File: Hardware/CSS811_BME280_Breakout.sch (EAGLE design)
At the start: 24 parts, among them J1 JST, J2 CCS811 Options, J3 JST, J4 PTH, U2 CCS811

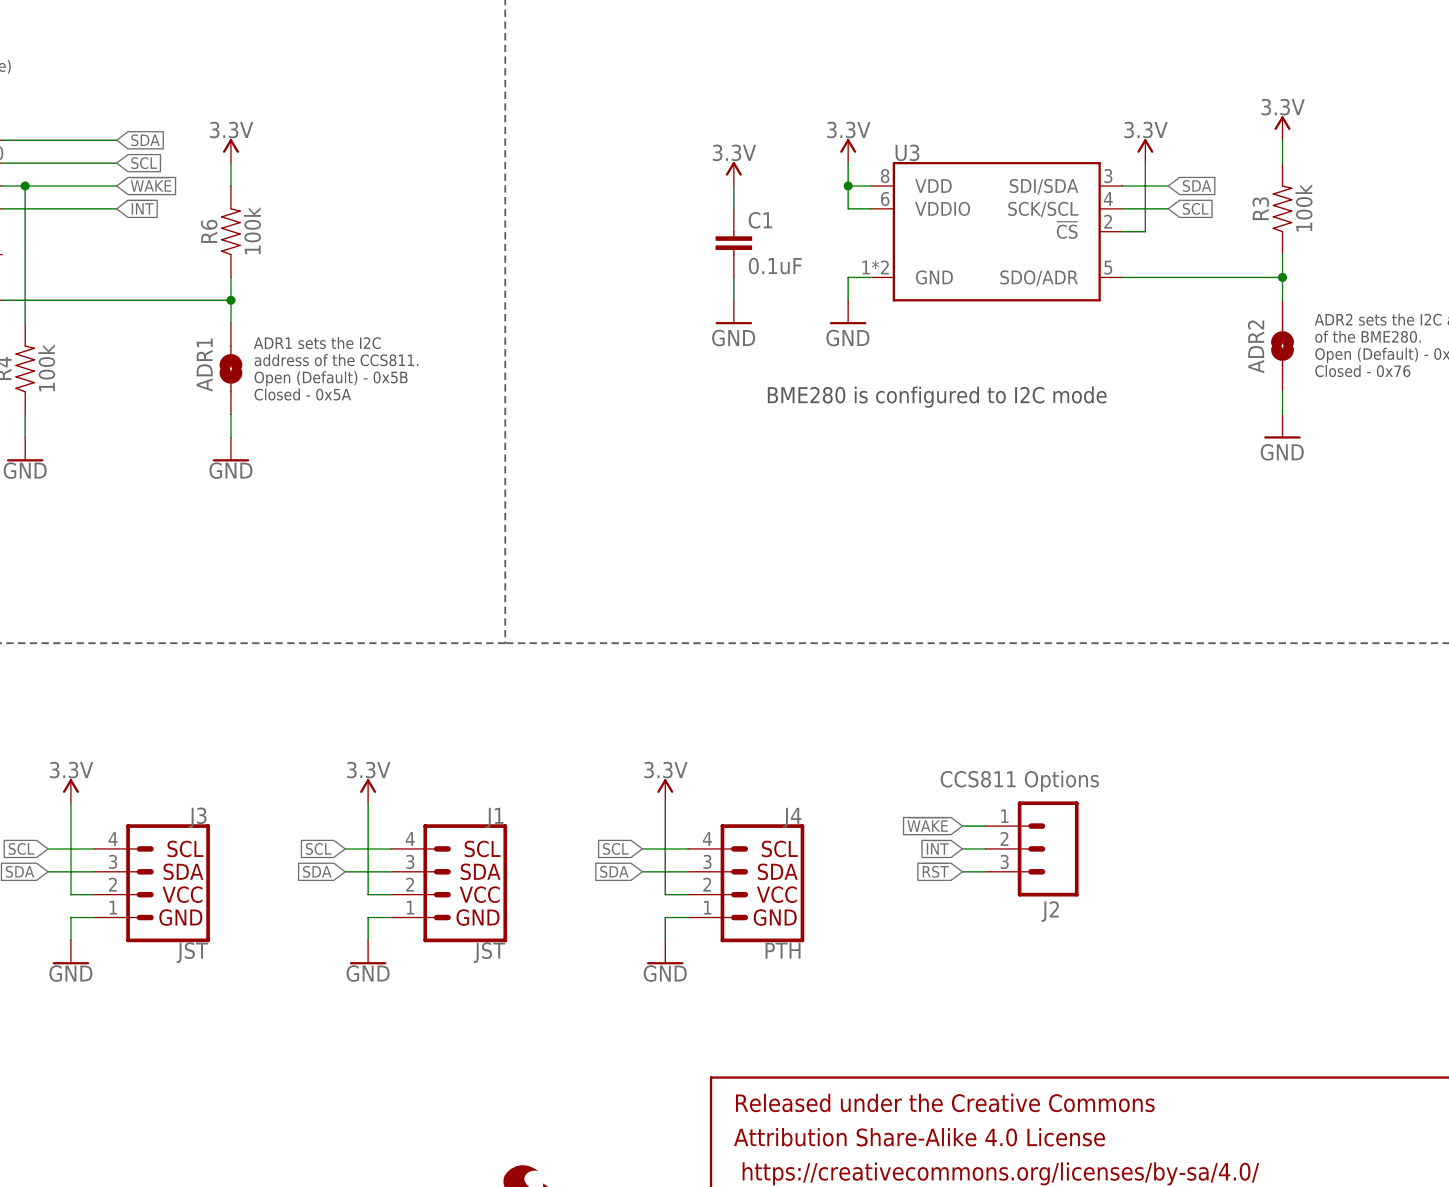
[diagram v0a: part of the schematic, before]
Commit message: Updated parts to fit with SFE library
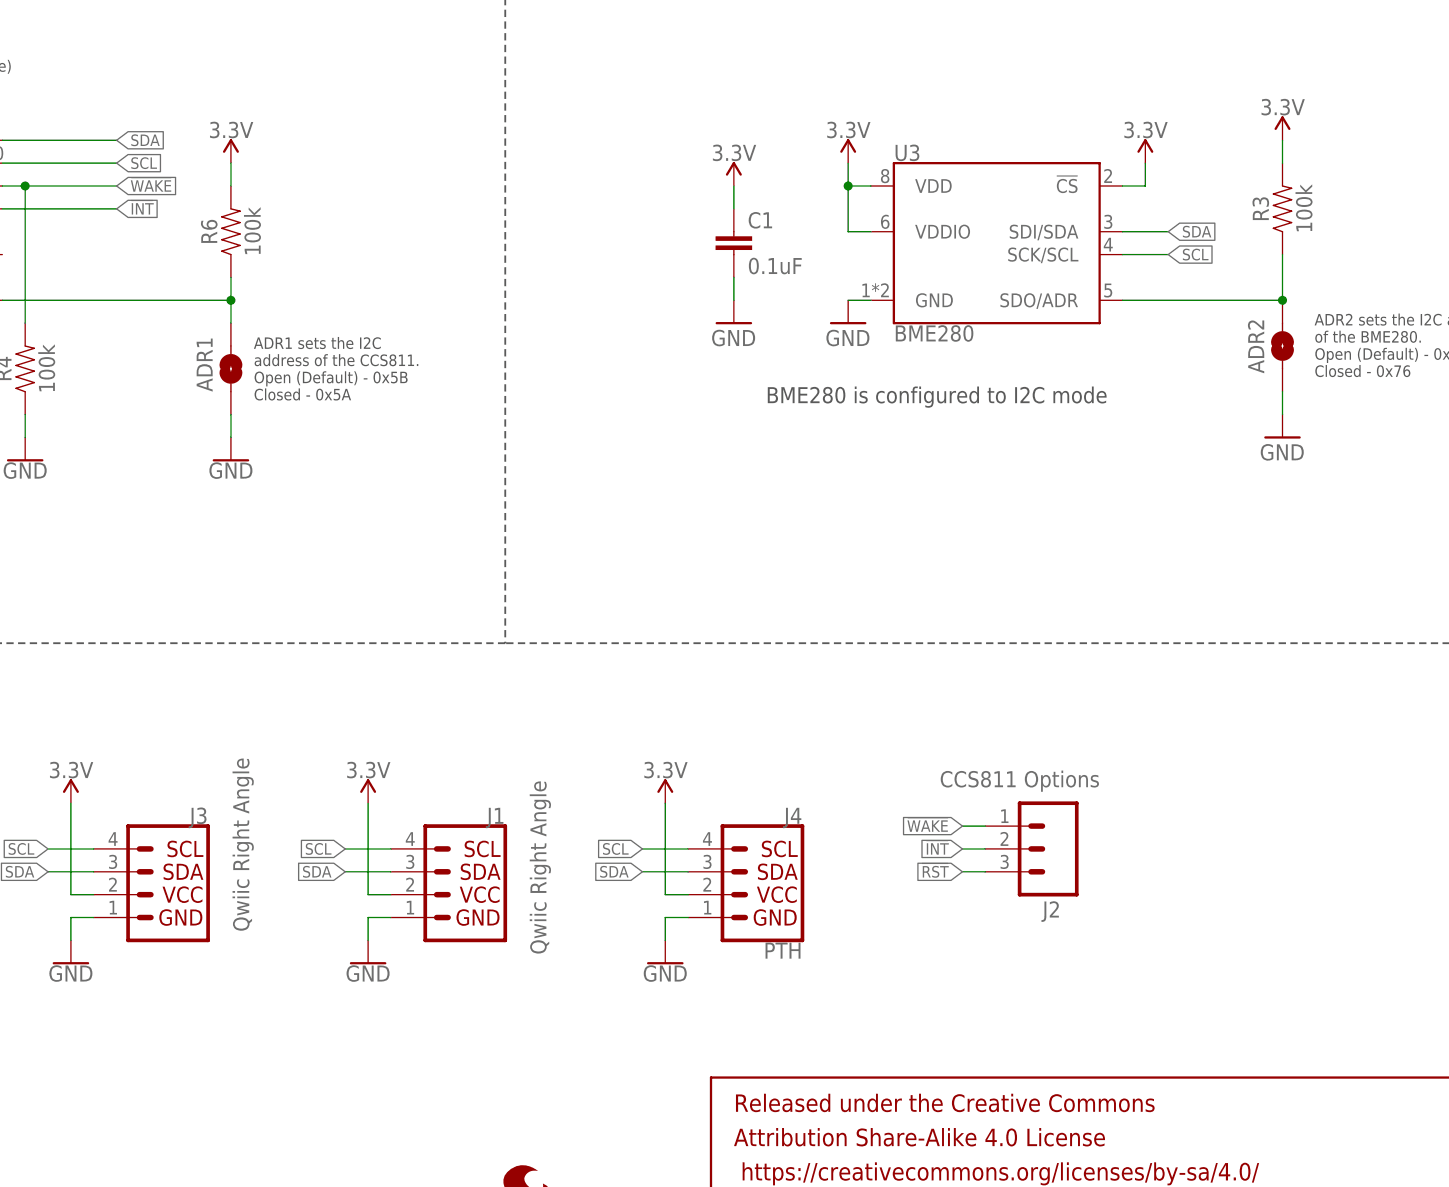
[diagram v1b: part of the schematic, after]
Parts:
- J1, J3: value JST -> Qwiic Right Angle; device SparkX:I2C_STANDARDJS-1MM -> SparkFun-Connectors:I2C_STANDARDQWIIC
- U2: device SparkX:CCS811PRODUCTION -> SparkFun-Sensors:CCS811PRODUCTION
- U3: value (none) -> BME280; device SparkX:BME280 -> SparkFun-Sensors:BME280
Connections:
- net 3.3V: now also J1.2, J3.2; no longer J1.VCC, J3.VCC
- net GND: now also J1.1, J3.1; no longer J1.GND, J3.GND
- net SCL: now also J1.4, J3.4; no longer J1.SCL, J3.SCL
- net SDA: now also J1.3, J3.3; no longer J1.SDA, J3.SDA
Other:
- moved on the sheet: U3
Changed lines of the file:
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@@
 <layer number="230" name="230bmp" color="7" fill="1" visible="yes" active="yes"/>
 <layer number="231" name="231bmp" color="7" fill="1" visible="yes" active="yes"/>
+<layer number="232" name="Eagle3D_PG2" color="7" fill="1" visible="yes" active="yes"/>
+<layer number="233" name="Eagle3D_PG3" color="7" fill="1" visible="yes" active="yes"/>
 <layer number="248" name="Housing" color="7" fill="1" visible="yes" active="yes"/>
 <layer number="249" name="Edge" color="7" fill="1" visible="yes" active="yes"/>
@@
 <part name="R2" library="SparkFun-Resistors" deviceset="4.7KOHM" device="-0603-1/10W-1%" value="4.7k"/>
 <part name="J2" library="SparkFun-Connectors" deviceset="CONN_03" device="1X03_NO_SILK" value="CCS811 Options"/>
-<part name="U2" library="SparkX" deviceset="CCS811" device="PRODUCTION" value="CCS811"/>
+<part name="U2" library="SparkFun-Sensors" deviceset="CCS811" device="PRODUCTION" value="CCS811"/>
 <part name="GND2" library="SparkFun-Aesthetics" deviceset="GND" device=""/>
 <part name="GND7" library="SparkFun-Aesthetics" deviceset="GND" device=""/>
@@
 <part name="SUPPLY12" library="SparkFun-PowerSymbols" deviceset="3.3V" device=""/>
 <part name="SUPPLY14" library="SparkFun-PowerSymbols" deviceset="3.3V" device=""/>
-<part name="U3" library="SparkX" deviceset="BME280" device=""/>
-<part name="J3" library="SparkX" deviceset="I2C_STANDARD" device="JS-1MM" value="JST"/>
+<part name="U3" library="SparkFun-Sensors" deviceset="BME280" device="" value="BME280"/>
+<part name="J3" library="SparkFun-Connectors" deviceset="I2C_STANDARD" device="QWIIC" value="Qwiic Right Angle"/>
 <part name="GND4" library="SparkFun-PowerSymbols" deviceset="GND" device=""/>
 <part name="SUPPLY1" library="SparkFun-PowerSymbols" deviceset="3.3V" device=""/>
@@
 <part name="GND1" library="SparkFun-PowerSymbols" deviceset="GND" device=""/>
 <part name="SUPPLY4" library="SparkFun-PowerSymbols" deviceset="3.3V" device=""/>
-<part name="J1" library="SparkX" deviceset="I2C_STANDARD" device="JS-1MM" value="JST"/>
+<part name="J1" library="SparkFun-Connectors" deviceset="I2C_STANDARD" device="QWIIC" value="Qwiic Right Angle"/>
 <part name="LOGO1" library="SparkFun-Aesthetics" deviceset="SFE_LOGO_NAME_FLAME" device=".1_INCH"/>
 </parts>
@@
 <instance part="SUPPLY14" gate="G$1" x="149.86" y="134.62"/>
 <instance part="U3" gate="U1" x="177.8" y="129.54"/>
-<instance part="J3" gate="G$1" x="86.36" y="55.88" rot="MR0"/>
+<instance part="J3" gate="G$1" x="86.36" y="55.88" smashed="yes" rot="MR0">
+<attribute name="VALUE" x="94.234" y="71.12" size="1.778" layer="96" font="vector" rot="MR270" align="top-left"/>
+<attribute name="NAME" x="91.44" y="63.754" size="1.778" layer="95" font="vector" rot="MR0"/>
+</instance>
 <instance part="GND4" gate="1" x="142.24" y="48.26" rot="MR0"/>
 <instance part="SUPPLY1" gate="G$1" x="142.24" y="66.04" rot="MR0"/>
@@
 <instance part="R4" gate="G$1" x="71.12" y="114.3" rot="R90"/>
 <instance part="GND5" gate="1" x="71.12" y="104.14"/>
-<instance part="GND1" gate="1" x="109.22" y="48.26" rot="MR0"/>
+<instance part="GND1" gate="1" x="109.22" y="48.26" smashed="yes" rot="MR0">
+<attribute name="VALUE" x="109.22" y="48.006" size="1.778" layer="96" rot="MR0" align="top-center"/>
+</instance>
 <instance part="SUPPLY4" gate="G$1" x="109.22" y="66.04" rot="MR0"/>
-<instance part="J1" gate="G$1" x="119.38" y="55.88" rot="MR0"/>
+<instance part="J1" gate="G$1" x="119.38" y="55.88" smashed="yes" rot="MR0">
+<attribute name="VALUE" x="127.254" y="68.58" size="1.778" layer="96" font="vector" rot="MR270" align="top-left"/>
+<attribute name="NAME" x="124.46" y="63.754" size="1.778" layer="95" font="vector" rot="MR0"/>
+</instance>
 <instance part="LOGO1" gate="G$1" x="88.9" y="0"/>
 </instances>
@@
 <wire x1="76.2" y1="53.34" x2="76.2" y2="50.8" width="0.1524" layer="91"/>
 <pinref part="GND18" gate="1" pin="GND"/>
-<pinref part="J3" gate="G$1" pin="GND"/>
+<pinref part="J3" gate="G$1" pin="1"/>
 </segment>
 <segment>
@@
 <pinref part="U3" gate="U1" pin="GND"/>
 <pinref part="GND2" gate="1" pin="GND"/>
-<wire x1="165.1" y1="124.46" x2="162.56" y2="124.46" width="0.1524" layer="91"/>
-<wire x1="162.56" y1="124.46" x2="162.56" y2="121.92" width="0.1524" layer="91"/>
+<wire x1="165.1" y1="121.92" x2="162.56" y2="121.92" width="0.1524" layer="91"/>
 </segment>
 <segment>
@@
 <wire x1="109.22" y1="53.34" x2="109.22" y2="50.8" width="0.1524" layer="91"/>
 <pinref part="GND1" gate="1" pin="GND"/>
-<pinref part="J1" gate="G$1" pin="GND"/>
+<pinref part="J1" gate="G$1" pin="1"/>
 </segment>
 </net>
@@
 <wire x1="78.74" y1="60.96" x2="73.66" y2="60.96" width="0.1524" layer="91"/>
 <label x="73.66" y="60.96" size="1.27" layer="95" rot="MR0" xref="yes"/>
-<pinref part="J3" gate="G$1" pin="SCL"/>
+<pinref part="J3" gate="G$1" pin="4"/>
 </segment>
 <segment>
@@
 </segment>
 <segment>
-<label x="198.12" y="132.08" size="1.27" layer="95" xref="yes"/>
-<wire x1="193.04" y1="132.08" x2="198.12" y2="132.08" width="0.1524" layer="91"/>
+<label x="198.12" y="127" size="1.27" layer="95" xref="yes"/>
+<wire x1="193.04" y1="127" x2="198.12" y2="127" width="0.1524" layer="91"/>
 <pinref part="U3" gate="U1" pin="SCK/SCL"/>
 </segment>
@@
 <wire x1="111.76" y1="60.96" x2="106.68" y2="60.96" width="0.1524" layer="91"/>
 <label x="106.68" y="60.96" size="1.27" layer="95" rot="MR0" xref="yes"/>
-<pinref part="J1" gate="G$1" pin="SCL"/>
+<pinref part="J1" gate="G$1" pin="4"/>
 </segment>
 </net>
@@
 <wire x1="78.74" y1="58.42" x2="73.66" y2="58.42" width="0.1524" layer="91"/>
 <label x="73.66" y="58.42" size="1.27" layer="95" rot="MR0" xref="yes"/>
-<pinref part="J3" gate="G$1" pin="SDA"/>
+<pinref part="J3" gate="G$1" pin="3"/>
 </segment>
 <segment>
@@
 </segment>
 <segment>
-<label x="198.12" y="134.62" size="1.27" layer="95" xref="yes"/>
-<wire x1="193.04" y1="134.62" x2="198.12" y2="134.62" width="0.1524" layer="91"/>
+<label x="198.12" y="129.54" size="1.27" layer="95" xref="yes"/>
+<wire x1="193.04" y1="129.54" x2="198.12" y2="129.54" width="0.1524" layer="91"/>
 <pinref part="U3" gate="U1" pin="SDI/SDA"/>
 </segment>
@@
 <wire x1="111.76" y1="58.42" x2="106.68" y2="58.42" width="0.1524" layer="91"/>
 <label x="106.68" y="58.42" size="1.27" layer="95" rot="MR0" xref="yes"/>
-<pinref part="J1" gate="G$1" pin="SDA"/>
+<pinref part="J1" gate="G$1" pin="3"/>
 </segment>
 </net>
@@
 <wire x1="76.2" y1="55.88" x2="76.2" y2="66.04" width="0.1524" layer="91"/>
 <pinref part="SUPPLY21" gate="G$1" pin="3.3V"/>
-<pinref part="J3" gate="G$1" pin="VCC"/>
+<pinref part="J3" gate="G$1" pin="2"/>
 </segment>
 <segment>
@@
 </segment>
 <segment>
-<wire x1="193.04" y1="129.54" x2="195.58" y2="129.54" width="0.1524" layer="91"/>
-<wire x1="195.58" y1="137.16" x2="195.58" y2="129.54" width="0.1524" layer="91"/>
+<wire x1="193.04" y1="134.62" x2="195.58" y2="134.62" width="0.1524" layer="91"/>
+<wire x1="195.58" y1="137.16" x2="195.58" y2="134.62" width="0.1524" layer="91"/>
 <pinref part="SUPPLY12" gate="G$1" pin="3.3V"/>
 <pinref part="U3" gate="U1" pin="!CS"/>
@@
 <pinref part="U3" gate="U1" pin="VDD"/>
 <pinref part="U3" gate="U1" pin="VDDIO"/>
-<wire x1="165.1" y1="132.08" x2="162.56" y2="132.08" width="0.1524" layer="91"/>
-<wire x1="162.56" y1="132.08" x2="162.56" y2="134.62" width="0.1524" layer="91"/>
+<wire x1="165.1" y1="129.54" x2="162.56" y2="129.54" width="0.1524" layer="91"/>
+<wire x1="162.56" y1="129.54" x2="162.56" y2="134.62" width="0.1524" layer="91"/>
 <junction x="162.56" y="134.62"/>
 </segment>
@@
 <wire x1="109.22" y1="55.88" x2="109.22" y2="66.04" width="0.1524" layer="91"/>
 <pinref part="SUPPLY4" gate="G$1" pin="3.3V"/>
-<pinref part="J1" gate="G$1" pin="VCC"/>
+<pinref part="J1" gate="G$1" pin="2"/>
 </segment>
 </net>
@@
 <pinref part="R3" gate="G$1" pin="1"/>
 <pinref part="ADR2" gate="G$1" pin="2"/>
-<wire x1="210.82" y1="121.92" x2="210.82" y2="124.46" width="0.1524" layer="91"/>
-<wire x1="210.82" y1="124.46" x2="210.82" y2="127" width="0.1524" layer="91"/>
-<wire x1="193.04" y1="124.46" x2="210.82" y2="124.46" width="0.1524" layer="91"/>
-<junction x="210.82" y="124.46"/>
+<wire x1="210.82" y1="121.92" x2="210.82" y2="127" width="0.1524" layer="91"/>
+<wire x1="193.04" y1="121.92" x2="210.82" y2="121.92" width="0.1524" layer="91"/>
+<junction x="210.82" y="121.92"/>
 <pinref part="U3" gate="U1" pin="SDO/ADR"/>
 </segment>

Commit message: Pre design review changes
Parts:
- added LOGO2: REVISION, SparkFun-Aesthetics:REVISION
- C1: device SparkFun-Capacitors:0.1UF-25V-5%(0603) -> SparkFun-Capacitors:0.1UF-0603-25V-(+80/-20%)
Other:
- note added: "Andrew England"
- note added: "V01"
- note removed: "X11"
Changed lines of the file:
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@@
 <part name="GND2" library="SparkFun-Aesthetics" deviceset="GND" device=""/>
 <part name="GND7" library="SparkFun-Aesthetics" deviceset="GND" device=""/>
-<part name="C1" library="SparkFun-Capacitors" deviceset="0.1UF-25V-5%(0603)" device="" value="0.1uF"/>
+<part name="C1" library="SparkFun-Capacitors" deviceset="0.1UF" device="-0603-25V-(+80/-20%)" value="0.1uF"/>
 <part name="GND8" library="SparkFun-Aesthetics" deviceset="GND" device=""/>
 <part name="R3" library="SparkFun-Resistors" deviceset="100KOHM" device="-0603-1/10W-1%" value="100k"/>
@@
 <part name="J1" library="SparkFun-Connectors" deviceset="I2C_STANDARD" device="QWIIC" value="Qwiic Right Angle"/>
 <part name="LOGO1" library="SparkFun-Aesthetics" deviceset="SFE_LOGO_NAME_FLAME" device=".1_INCH"/>
+<part name="LOGO2" library="SparkFun-Aesthetics" deviceset="REVISION" device=""/>
 </parts>
 <sheets>
@@
 to 4.7k pull-up
 resistors.</text>
-<text x="238.76" y="7.62" size="2.54" layer="94" align="center-left">X11</text>
+<text x="238.76" y="7.62" size="2.54" layer="94" align="center-left">V01</text>
 <text x="170.688" y="12.446" size="2.54" layer="94" align="center-left">Nathan Seidle</text>
 <text x="214.376" y="120.396" size="1.27" layer="97" align="top-left">ADR2 sets the I2C address
@@
 <wire x1="124.46" y1="83.82" x2="0" y2="83.82" width="0.2032" layer="97" style="longdash"/>
 <wire x1="124.46" y1="185.42" x2="124.46" y2="83.82" width="0.2032" layer="97" style="longdash"/>
+<text x="174.752" y="6.858" size="2.54" layer="94">Andrew England</text>
 </plain>
 <instances>
@@
 </instance>
 <instance part="LOGO1" gate="G$1" x="88.9" y="0"/>
+<instance part="LOGO2" gate="G$1" x="148.59" y="6.858"/>
 </instances>
 <busses>

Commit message: Added Dimensions
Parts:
- LOGO1: value SFE_LOGO_NAME_FLAME.1_INCH -> SFE_LOGO_NAME.1_INCH; device SparkFun-Aesthetics:SFE_LOGO_NAME_FLAME.1_INCH -> SparkFun-Aesthetics:SFE_LOGO_NAME.1_INCH
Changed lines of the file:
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@@
 <part name="SUPPLY4" library="SparkFun-PowerSymbols" deviceset="3.3V" device=""/>
 <part name="J1" library="SparkFun-Connectors" deviceset="I2C_STANDARD" device="QWIIC" value="Qwiic Right Angle"/>
-<part name="LOGO1" library="SparkFun-Aesthetics" deviceset="SFE_LOGO_NAME_FLAME" device=".1_INCH"/>
 <part name="LOGO2" library="SparkFun-Aesthetics" deviceset="REVISION" device=""/>
+<part name="LOGO1" library="SparkFun-Aesthetics" deviceset="SFE_LOGO_NAME" device=".1_INCH"/>
 </parts>
 <sheets>
@@
 <attribute name="NAME" x="124.46" y="63.754" size="1.778" layer="95" font="vector" rot="MR0"/>
 </instance>
-<instance part="LOGO1" gate="G$1" x="88.9" y="0"/>
 <instance part="LOGO2" gate="G$1" x="148.59" y="6.858"/>
+<instance part="LOGO1" gate="G$1" x="88.9" y="2.54"/>
 </instances>
 <busses>

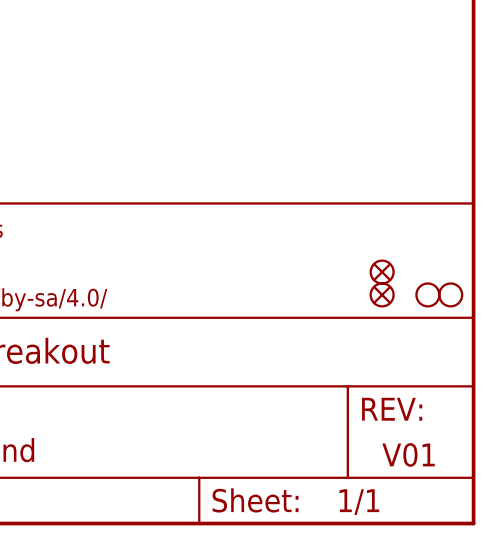
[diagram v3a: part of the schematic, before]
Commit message: Added fiducials to bottom of board
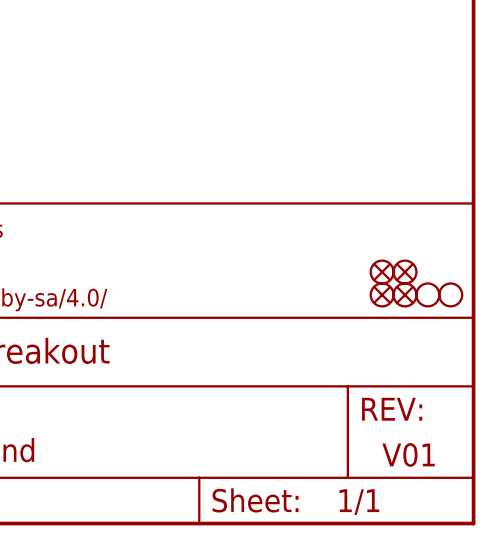
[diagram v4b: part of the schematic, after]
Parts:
- added FD3, FD4: FIDUCIAL1X2, SparkFun-Aesthetics:FIDUCIAL1X2
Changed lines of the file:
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@@
 <part name="LOGO2" library="SparkFun-Aesthetics" deviceset="REVISION" device=""/>
 <part name="LOGO1" library="SparkFun-Aesthetics" deviceset="SFE_LOGO_NAME" device=".1_INCH"/>
+<part name="FD3" library="SparkFun-Aesthetics" deviceset="FIDUCIAL" device="1X2"/>
+<part name="FD4" library="SparkFun-Aesthetics" deviceset="FIDUCIAL" device="1X2"/>
 </parts>
 <sheets>
@@
 <instance part="LOGO2" gate="G$1" x="148.59" y="6.858"/>
 <instance part="LOGO1" gate="G$1" x="88.9" y="2.54"/>
+<instance part="FD3" gate="G$1" x="241.3" y="27.94"/>
+<instance part="FD4" gate="G$1" x="241.3" y="25.4"/>
 </instances>
 <busses>
